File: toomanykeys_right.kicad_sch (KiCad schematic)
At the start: 81 parts, among them U1 TLV61070ADBV, U2 SN74LV1T126DBVR

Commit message: Fully route left half. Schematic and PCB both clean!
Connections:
- net LCD_BL: now also MCU1.15 (P0.11); no longer MCU1.18 (P0.22)
- net LCD_CLK: now also MCU1.17 (P0.24); no longer MCU1.16 (P1.00)
- net LCD_DC: now also MCU1.16 (P1.00); no longer MCU1.17 (P0.24)
- net LCD_DIN: now also MCU1.18 (P0.22); no longer MCU1.15 (P0.11)
- net RAW: now also PWR1.1 (A); no longer PWR1.3 (C)
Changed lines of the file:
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@@
 	)
 	(no_connect
-		(at 69.85 137.16)
+		(at 69.85 132.08)
 	)
 	(wire
@@
 		)
 	)
-	(global_label "LCD_CLK"
+	(global_label "R0"
 		(shape input)
-		(at 33.02 167.64 180)
+		(at 33.02 157.48 180)
 		(fields_autoplaced yes)
 		(effects
@@
 		)
 		(property "Intersheetrefs" "${INTERSHEET_REFS}"
-			(at 21.931 167.64 0)
+			(at 27.5553 157.48 0)
 			(effects
 				(font
@@
 		)
 	)
-	(global_label "R0"
+	(global_label "LCD_CLK"
 		(shape input)
-		(at 33.02 157.48 180)
+		(at 33.02 165.1 180)
 		(fields_autoplaced yes)
 		(effects
@@
 		)
 		(property "Intersheetrefs" "${INTERSHEET_REFS}"
-			(at 27.5553 157.48 0)
+			(at 21.931 165.1 0)
 			(effects
 				(font
@@
 	(global_label "LCD_BL"
 		(shape input)
-		(at 137.16 158.75 90)
+		(at 33.02 170.18 180)
 		(fields_autoplaced yes)
 		(effects
@@
 				(size 1.27 1.27)
 			)
-			(justify left)
+			(justify right)
 		)
 		(property "Intersheetrefs" "${INTERSHEET_REFS}"
-			(at 137.16 148.931 90)
+			(at 23.201 170.18 0)
 			(effects
 				(font
 					(size 1.27 1.27)
 				)
-				(justify left)
+				(justify right)
 				(hide yes)
 			)
 		)
 	)
-	(global_label "C2"
+	(global_label "LCD_BL"
 		(shape input)
-		(at 99.06 21.59 90)
+		(at 137.16 158.75 90)
 		(fields_autoplaced yes)
 		(effects
@@
 		)
 		(property "Intersheetrefs" "${INTERSHEET_REFS}"
-			(at 99.06 16.1253 90)
+			(at 137.16 148.931 90)
 			(effects
 				(font
@@
 		)
 	)
-	(global_label "R1"
+	(global_label "C2"
 		(shape input)
-		(at 38.1 48.26 180)
+		(at 99.06 21.59 90)
 		(fields_autoplaced yes)
 		(effects
@@
 				(size 1.27 1.27)
 			)
-			(justify right)
+			(justify left)
 		)
 		(property "Intersheetrefs" "${INTERSHEET_REFS}"
-			(at 32.6353 48.26 0)
+			(at 99.06 16.1253 90)
 			(effects
 				(font
 					(size 1.27 1.27)
 				)
-				(justify right)
+				(justify left)
 				(hide yes)
 			)
 		)
 	)
-	(global_label "LCD_BL"
+	(global_label "R1"
 		(shape input)
-		(at 33.02 162.56 180)
+		(at 38.1 48.26 180)
 		(fields_autoplaced yes)
 		(effects
@@
 		)
 		(property "Intersheetrefs" "${INTERSHEET_REFS}"
-			(at 23.201 162.56 0)
+			(at 32.6353 48.26 0)
 			(effects
 				(font
@@
 		)
 	)
-	(global_label "LCD_DC"
-		(shape input)
-		(at 33.02 165.1 180)
-		(fields_autoplaced yes)
-		(effects
-			(font
-				(size 1.27 1.27)
-			)
-			(justify right)
-		)
-		(property "Intersheetrefs" "${INTERSHEET_REFS}"
-			(at 22.9591 165.1 0)
-			(effects
-				(font
-					(size 1.27 1.27)
-				)
-				(justify right)
-				(hide yes)
-			)
-		)
-	)
 	(global_label "RAW"
 		(shape input)
@@
 		)
 	)
+	(global_label "RAW"
+		(shape input)
+		(at 69.85 137.16 180)
+		(fields_autoplaced yes)
+		(effects
+			(font
+				(size 1.27 1.27)
+			)
+			(justify right)
+		)
+		(property "Intersheetrefs" "${INTERSHEET_REFS}"
+			(at 63.0548 137.16 0)
+			(effects
+				(font
+					(size 1.27 1.27)
+				)
+				(justify right)
+				(hide yes)
+			)
+		)
+	)
 	(global_label "R2"
 		(shape input)
@@
 		)
 	)
+	(global_label "LCD_DC"
+		(shape input)
+		(at 33.02 167.64 180)
+		(fields_autoplaced yes)
+		(effects
+			(font
+				(size 1.27 1.27)
+			)
+			(justify right)
+		)
+		(property "Intersheetrefs" "${INTERSHEET_REFS}"
+			(at 22.9591 167.64 0)
+			(effects
+				(font
+					(size 1.27 1.27)
+				)
+				(justify right)
+				(hide yes)
+			)
+		)
+	)
 	(global_label "C1"
 		(shape input)
@@
 	(global_label "LCD_DIN"
 		(shape input)
-		(at 33.02 170.18 180)
-		(fields_autoplaced yes)
-		(effects
-			(font
-				(size 1.27 1.27)
-			)
-			(justify right)
-		)
-		(property "Intersheetrefs" "${INTERSHEET_REFS}"
-			(at 22.2938 170.18 0)
-			(effects
-				(font
-					(size 1.27 1.27)
-				)
-				(justify right)
-				(hide yes)
-			)
-		)
-	)
-	(global_label "RAW"
-		(shape input)
-		(at 69.85 132.08 180)
+		(at 33.02 162.56 180)
 		(fields_autoplaced yes)
 		(effects
@@
 		)
 		(property "Intersheetrefs" "${INTERSHEET_REFS}"
-			(at 63.0548 132.08 0)
+			(at 22.2938 162.56 0)
 			(effects
 				(font

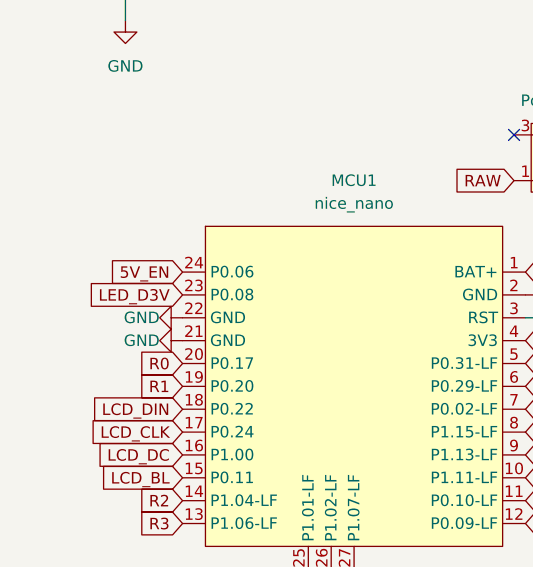
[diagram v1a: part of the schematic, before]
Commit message: Route right half. Make minor improvements on left. Ready for production?
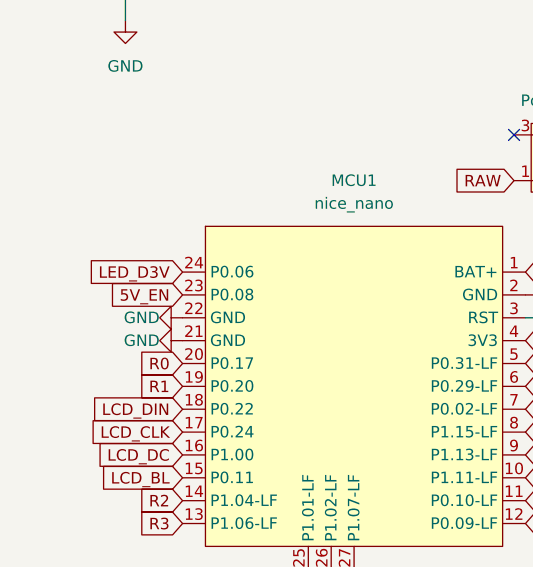
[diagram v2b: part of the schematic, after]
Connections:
- net 5V_EN: now also MCU1.23 (P0.08); no longer MCU1.24 (P0.06)
- net LED_D3V: now also MCU1.24 (P0.06); no longer MCU1.23 (P0.08)
